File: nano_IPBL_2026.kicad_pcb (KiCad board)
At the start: 2 copper layers, 44 x 85 mm, 21 parts, among them J1 DB301V-5.0-2P, M1 Motor_Servo, M10 Motor_Servo, M11 Motor_Servo, M12 Motor_Servo, M2 Motor_Servo, M3 Motor_Servo, M4 Motor_Servo, M5 Motor_Servo, M6 Motor_Servo, M7 Motor_Servo, M8 Motor_Servo, M9 Motor_Servo

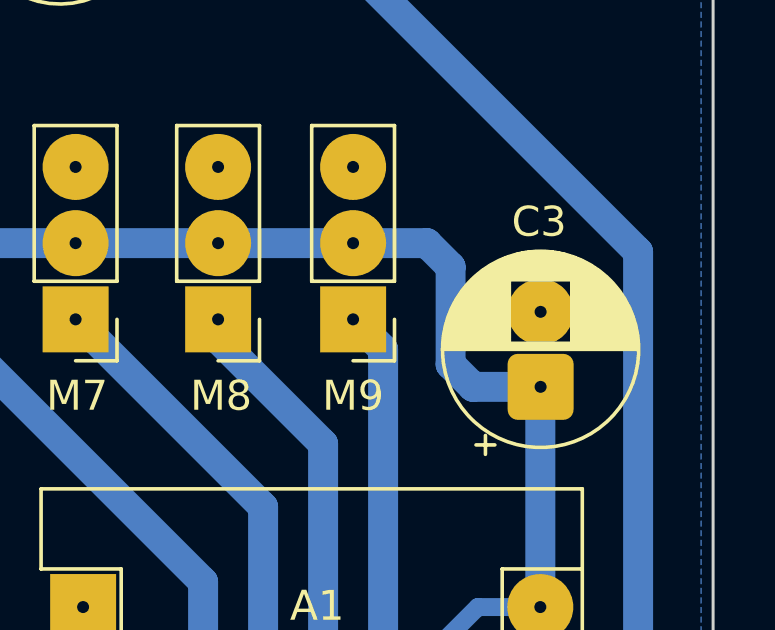
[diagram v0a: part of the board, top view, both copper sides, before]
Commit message: Add net labels to schematic for improved readability
Co-Authored-By: Claude Haiku 4.5 <noreply@anthropic.com>
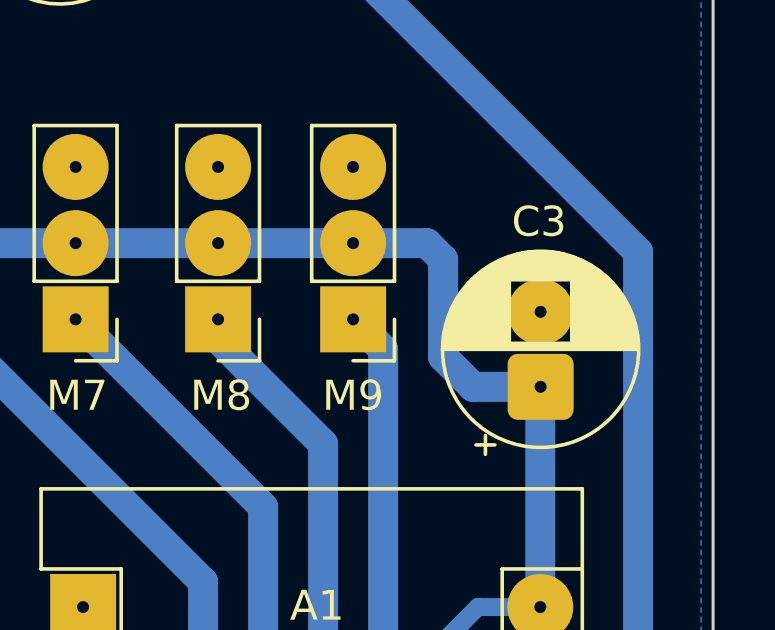
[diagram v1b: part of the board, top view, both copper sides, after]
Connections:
- net Net-(A1-D10) renamed /D10
- net Net-(A1-D11) renamed /D11
- net Net-(A1-D12) renamed /D12
- net Net-(A1-D13) renamed /D13
- net Net-(A1-D3) renamed /D3
- net Net-(A1-D4) renamed /D4
- net Net-(A1-D5) renamed /D5
- net Net-(A1-D6) renamed /D6
- net Net-(A1-D7) renamed /D7
- net Net-(A1-D8) renamed /D8
- net Net-(A1-D9) renamed /D9
- net Net-(A1-VIN) renamed /Servo_IN
